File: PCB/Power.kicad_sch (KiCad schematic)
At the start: 19 parts, among them U201 TPS5430DDA, U202 XC6206PxxxMR

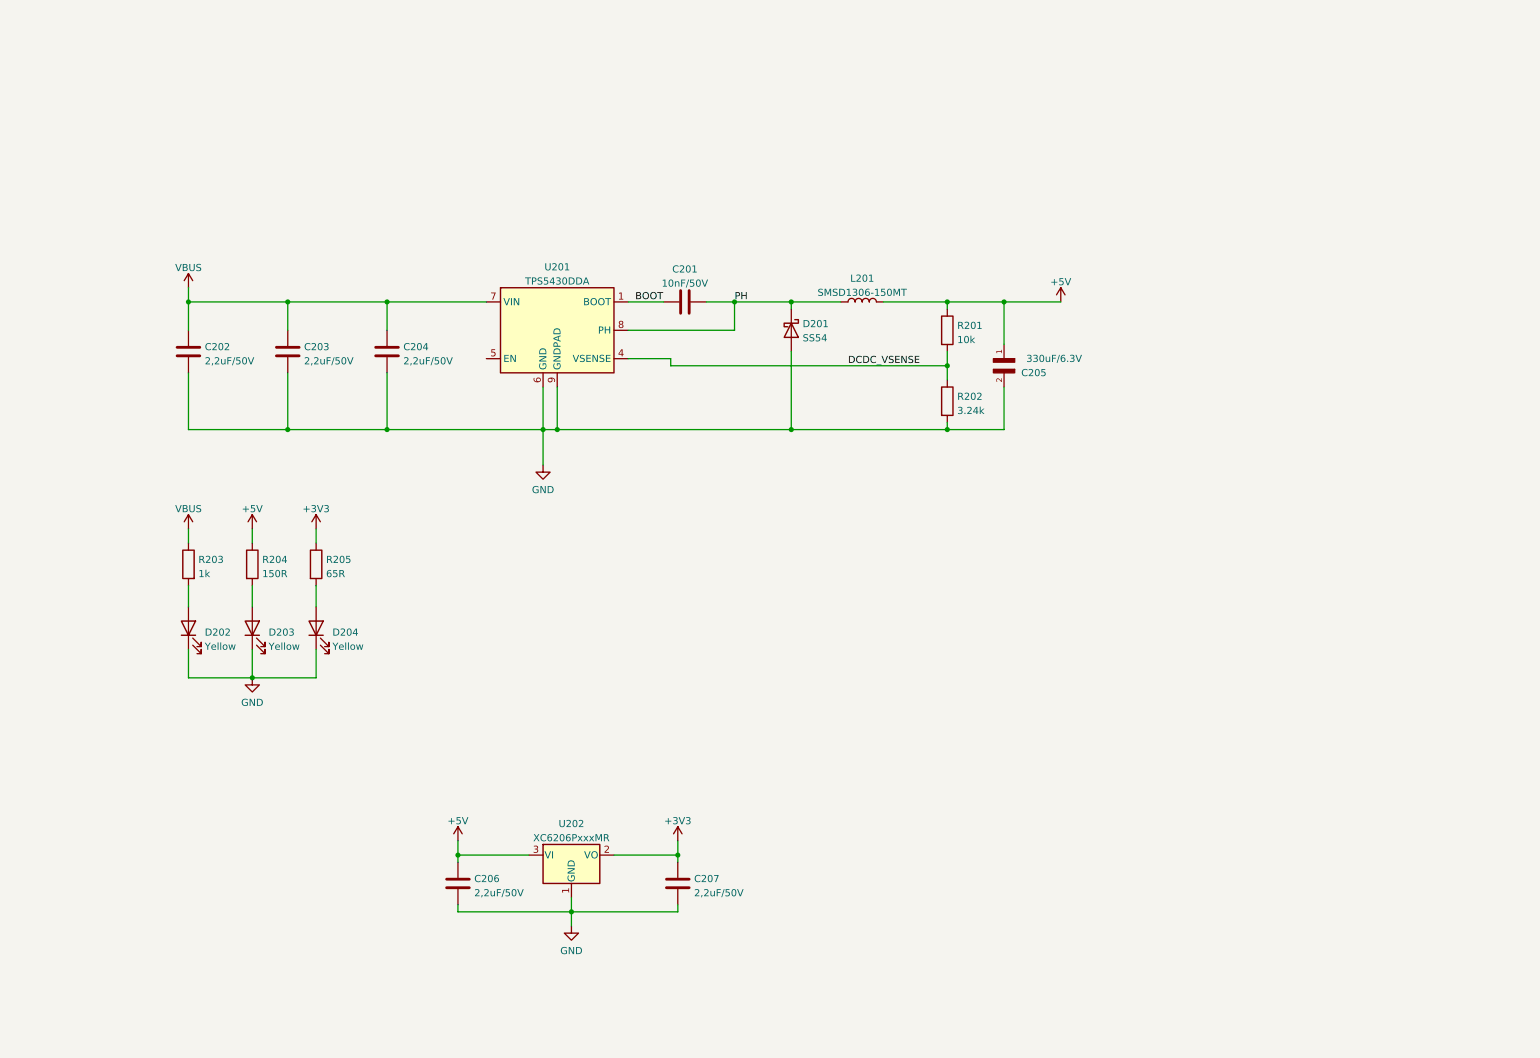
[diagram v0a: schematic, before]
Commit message: Add a new DC/DC solution to the schematic
Components has been added to layout, but not properly done
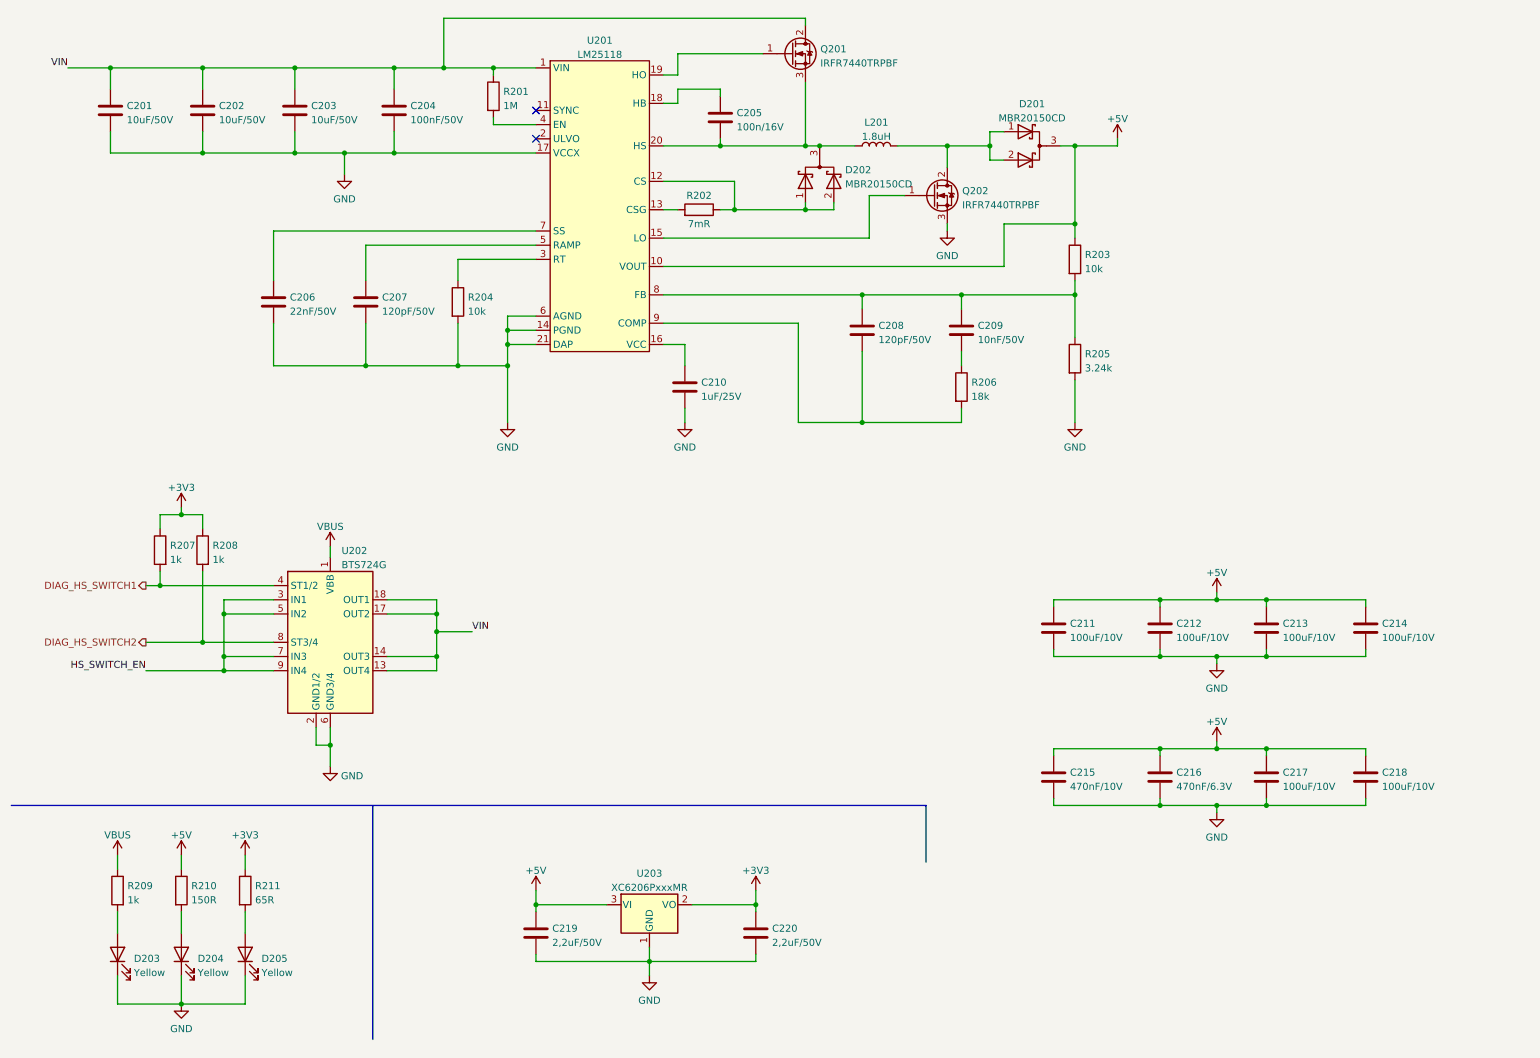
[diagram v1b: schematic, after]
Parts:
- removed C205: 330uF/6.3V, CAPPM7343X310N, symbol Skrooter_symbols:T520D337M006ATE025
- removed D201: SS54, Diode_SMD:D_SMA, symbol Device:D_Schottky
- removed U201: TPS5430DDA, Package_SO:TI_SO-PowerPAD-8_ThermalVias, symbol Regulator_Switching:TPS5430DDA
- added C205: 100n/16V, Capacitor_SMD:C_0402_1005Metric, symbol Device:C
- added C206: 22nF/50V, Capacitor_SMD:C_0402_1005Metric, symbol Device:C
- added C207, C208: 120pF/50V, Capacitor_SMD:C_0402_1005Metric, symbol Device:C
- added C209: 10nF/50V, Capacitor_SMD:C_0402_1005Metric, symbol Device:C
- added C210: 1uF/25V, Capacitor_SMD:C_0402_1005Metric, symbol Device:C
- added C211, C212, C213, C214, C217, C218: 100uF/10V, Capacitor_SMD:C_1206_3216Metric, symbol Device:C
- added C215: 470nF/10V, Capacitor_SMD:C_0402_1005Metric, symbol Device:C
- added C216: 470nF/6.3V, Capacitor_SMD:C_0402_1005Metric, symbol Device:C
- added D201, D202: MBR20150CD, Package_TO_SOT_SMD:TO-252-2, symbol Device:D_Schottky_Dual_CommonCathode_AAK_Parallel
- added Q201, Q202: IRFR7440TRPBF, Package_TO_SOT_SMD:TO-252-2, symbol Device:Q_NMOS_GDS
- added R203, R204: 10k, Resistor_SMD:R_0402_1005Metric, symbol Device:R
- added R205: 3.24k, Resistor_SMD:R_0402_1005Metric, symbol Device:R
- added R206: 18k, Resistor_SMD:R_0402_1005Metric, symbol Device:R
- added R207, R208: 1k, Resistor_SMD:R_0402_1005Metric, symbol Device:R
- added U201: LM25118, Package_SO:HTSSOP-20-1EP_4.4x6.5mm_P0.65mm_EP3.4x6.5mm_Mask2.75x3.43mm_ThermalVias, symbol Skrooter_symbols:LM25118
- added U202: BTS724G, Package_SO:Infineon_PG-DSO-20-32, symbol Power_Management:BTS724G
- C201: value 10nF/50V -> 10uF/50V; footprint Capacitor_SMD:C_0402_1005Metric -> Capacitor_SMD:C_0805_2012Metric; LCSC C15195 -> C440198
- C202, C203: value 2,2uF/50V -> 10uF/50V; LCSC C49217 -> C440198
- C204: value 2,2uF/50V -> 100nF/50V; footprint Capacitor_SMD:C_0805_2012Metric -> Capacitor_SMD:C_0402_1005Metric; LCSC C49217 -> C307331
- D203: renamed from D202; LCSC (none) -> C72038
- D204: renamed from D203; LCSC (none) -> C72038
- D205: renamed from D204; LCSC (none) -> C72038
- L201: value SMSD1306-150MT -> 1.8uH; footprint Inductor_SMD:L_Bourns_SDR1806 -> Inductor_SMD:L_12x12mm_H8mm; LCSC C33624 -> C718301
- R201: value 10k -> 1M; LCSC C25744 -> C26083
- R202: value 3.24k -> 7mR; footprint Resistor_SMD:R_0402_1005Metric -> Resistor_SMD:R_2512_6332Metric; LCSC C25890 -> C728341
- renumbered C206 to C219, C207 to C220, R203 to R209, R204 to R210, R205 to R211, U202 to U203
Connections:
- net +3V3: now also R207.1, R208.1
- net +5V: now also C211.1, C212.1, C213.1, C214.1, C215.1, C216.1, C217.1, C218.1, D201.3 (A), R203.1, U201.10 (VOUT); no longer L201.2, R201.1
- net GND: now also C201.2, C206.2, C207.2, C210.2, C211.2, C212.2, C213.2, C214.2, C215.2, C216.2, C217.2, C218.2, Q202.3 (S), R204.2, R205.2, U201.14 (PGND), U201.17 (VCCX), U201.21 (DAP), U201.6 (AGND), U202.2 (GND1/2), U202.6 (GND3/4); no longer R202.2
- net VBUS: now also U202.1 (VBB), U202.10 (VBB), U202.11 (VBB), U202.12 (VBB), U202.15 (VBB), U202.16 (VBB), U202.19 (VBB), U202.20 (VBB); no longer C202.1, C203.1, C204.1
- net BOOT renamed VIN
- net VIN: now also C202.1, C203.1, C204.1, R201.1, Q201.2 (D), U201.1 (VIN), U202.13 (OUT4), U202.14 (OUT3), U202.17 (OUT2), U202.18 (OUT1)
- net DCDC_VSENSE: no longer names the net of R202.1
- net DCDC_VSENSE: now also D202.1 (K), D202.2 (K), U201.12 (CS); no longer R201.2
- net PH: no longer names the net of L201.1
- net PH: now also C205.2, D202.3 (A), Q201.3 (S), U201.20 (HS); no longer C201.2
- new net: D201.1 (K), D201.2 (K), L201.2, Q202.2 (D)
- new net: C208.1, C209.1, R203.2, R205.1, U201.8 (FB)
- new net: Q202.1 (G), U201.15 (LO)
- new net: C208.2, R206.2, U201.9 (COMP)
- new net: C209.2, R206.1
- new net: C207.1, U201.5 (RAMP)
- new net: R202.2, U201.13 (CSG)
- new net: R204.1, U201.3 (RT)
- new net: C205.1, U201.18 (HB)
- new net: C206.1, U201.7 (SS)
- new net: C210.1, U201.16 (VCC)
- new net: R201.2, U201.4 (EN)
- new net: Q201.1 (G), U201.19 (HO)
- new net DIAG_HS_SWITCH1: R207.2, U202.4 (ST1/2)
- new net DIAG_HS_SWITCH2: R208.2, U202.8 (ST3/4)
- new net HS_SWITCH_EN: U202.3 (IN1), U202.5 (IN2), U202.7 (IN3), U202.9 (IN4)
- no-connect marks 0 -> 2
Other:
- moved on the sheet: C219, C220, D203, D204, D205, R209, R210, R211, U203

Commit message: reroute pretty much everything
Routing is done for new DC/DC!
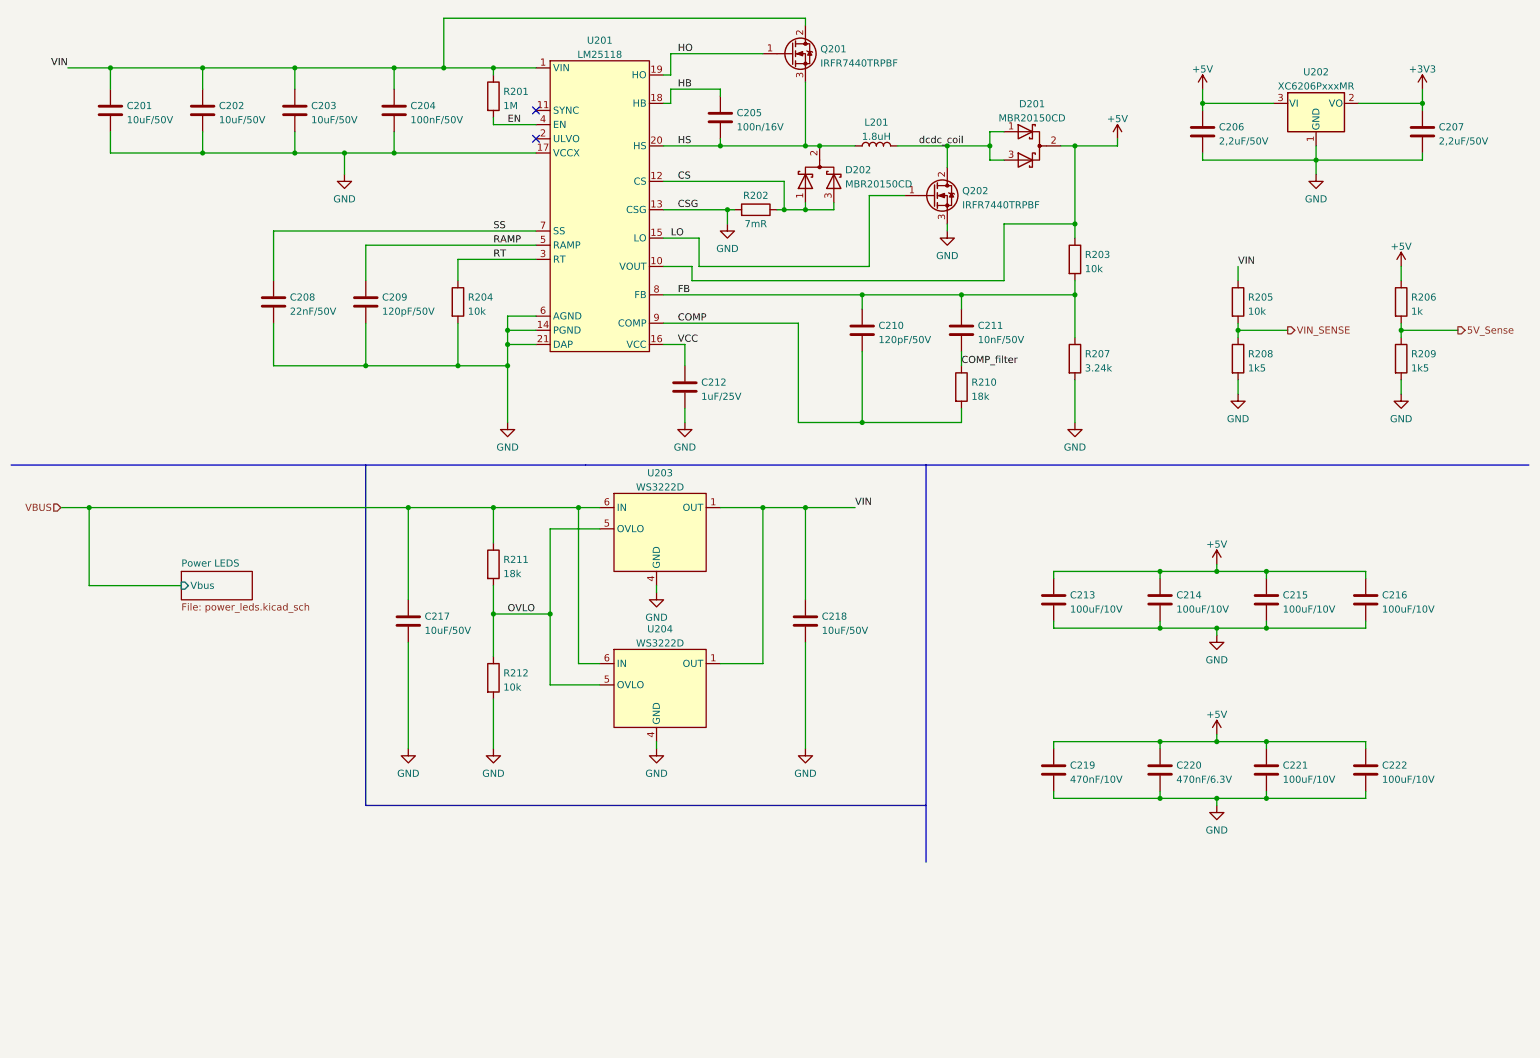
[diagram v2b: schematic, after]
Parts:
- removed D203, D204, D205: Yellow, LED_SMD:LED_0603_1608Metric, symbol Device:LED
- removed R207: 1k, Resistor_SMD:R_0402_1005Metric, symbol Device:R
- removed R210: 150R, Resistor_SMD:R_0402_1005Metric, symbol Device:R
- removed U202: BTS724G, Package_SO:Infineon_PG-DSO-20-32, symbol Power_Management:BTS724G
- added C217, C218: 10uF/50V, Capacitor_SMD:C_0805_2012Metric, symbol Device:C
- added R205, R212: 10k, Resistor_SMD:R_0402_1005Metric, symbol Device:R
- added R206: 1k, Resistor_SMD:R_0402_1005Metric, symbol Device:R
- added U203, U204: WS3222D, Package_DFN_QFN:WDFN-8-1EP_2x2mm_P0.5mm_EP0.8x1.2mm, symbol Skrooter_symbols:WS3222D
- D201, D202: symbol Device:D_Schottky_Dual_CommonCathode_AAK_Parallel -> Device:D_Schottky_Dual_CommonCathode_AKA_Parallel
- R208, R209: value 1k -> 1k5; LCSC C11702 -> C105871
- R211: value 65R -> 18k; footprint Resistor_SMD:R_0603_1608Metric -> Resistor_SMD:R_0402_1005Metric; LCSC C27592 -> C25762
- renumbered C219 to C206, C220 to C207, C206 to C208, C207 to C209, C208 to C210, C209 to C211, C210 to C212, C211 to C213, C212 to C214, C213 to C215, C214 to C216, C215 to C219, C216 to C220, C217 to C221, C218 to C222, R205 to R207, R206 to R210, U203 to U202
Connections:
- net DIAG_HS_SWITCH2 is gone; now on net GND: R208.2
- net +3V3: no longer R208.1, R211.1
- net +5V: now also D201.2 (A), R206.1; no longer D201.3 (A)
- net GND: now also R202.2, R209.2, U201.13 (CSG), C217.2, C218.2, R212.2, U203.4 (GND), U203.9 (GND), U204.4 (GND), U204.9 (GND)
- net VIN: now also C218.1, R205.1, U203.1 (OUT), U203.2 (OUT), U203.3 (OUT), U204.1 (OUT), U204.2 (OUT), U204.3 (OUT)
- net dcdc_coil: now reaches D201.1 (K), L201.2, Q202.2 (D)
- net dcdc_coil: now also D201.3 (K); no longer D201.2 (K)
- net FB: now reaches C210.1, C211.1, R203.2, R207.1, U201.8 (FB)
- net LO: now reaches Q202.1 (G), U201.15 (LO)
- net HS: now reaches C205.2, L201.1, Q201.3 (S), U201.20 (HS)
- net HS: now also D202.2 (A); no longer D202.3 (A)
- net COMP: now reaches C210.2, R210.2, U201.9 (COMP)
- net CS: now reaches D202.1 (K), R202.1, U201.12 (CS)
- net CS: now also D202.3 (K); no longer D202.2 (K)
- net OVLO: now reaches R211.2
- net OVLO: now also R212.1, U203.5 (OVLO), U204.5 (OVLO)
- net COMP_filter: now reaches C211.2, R210.1
- net RAMP: now reaches C209.1, U201.5 (RAMP)
- net RT: now reaches R204.1, U201.3 (RT)
- net HB: now reaches C205.1, U201.18 (HB)
- net SS: now reaches C208.1, U201.7 (SS)
- net VCC: now reaches C212.1, U201.16 (VCC)
- net EN: now reaches R201.2, U201.4 (EN)
- net HO: now reaches Q201.1 (G), U201.19 (HO)
- net VBUS renamed 5V_Sense
- net 5V_Sense: now also R206.2
- new net IN: C217.1, R211.1, U203.6 (IN), U203.7 (IN), U203.8 (IN), U204.6 (IN), U204.7 (IN), U204.8 (IN)
- new net VIN_SENSE: R205.2, R208.1
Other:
- added sheet Power LEDS (power_leds.kicad_sch)
- moved on the sheet: C206, C207, C213, C214, C215, C216, C219, C220, C221, C222, R202, U202

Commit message: Add LEDs for each USBPD level and a microphone
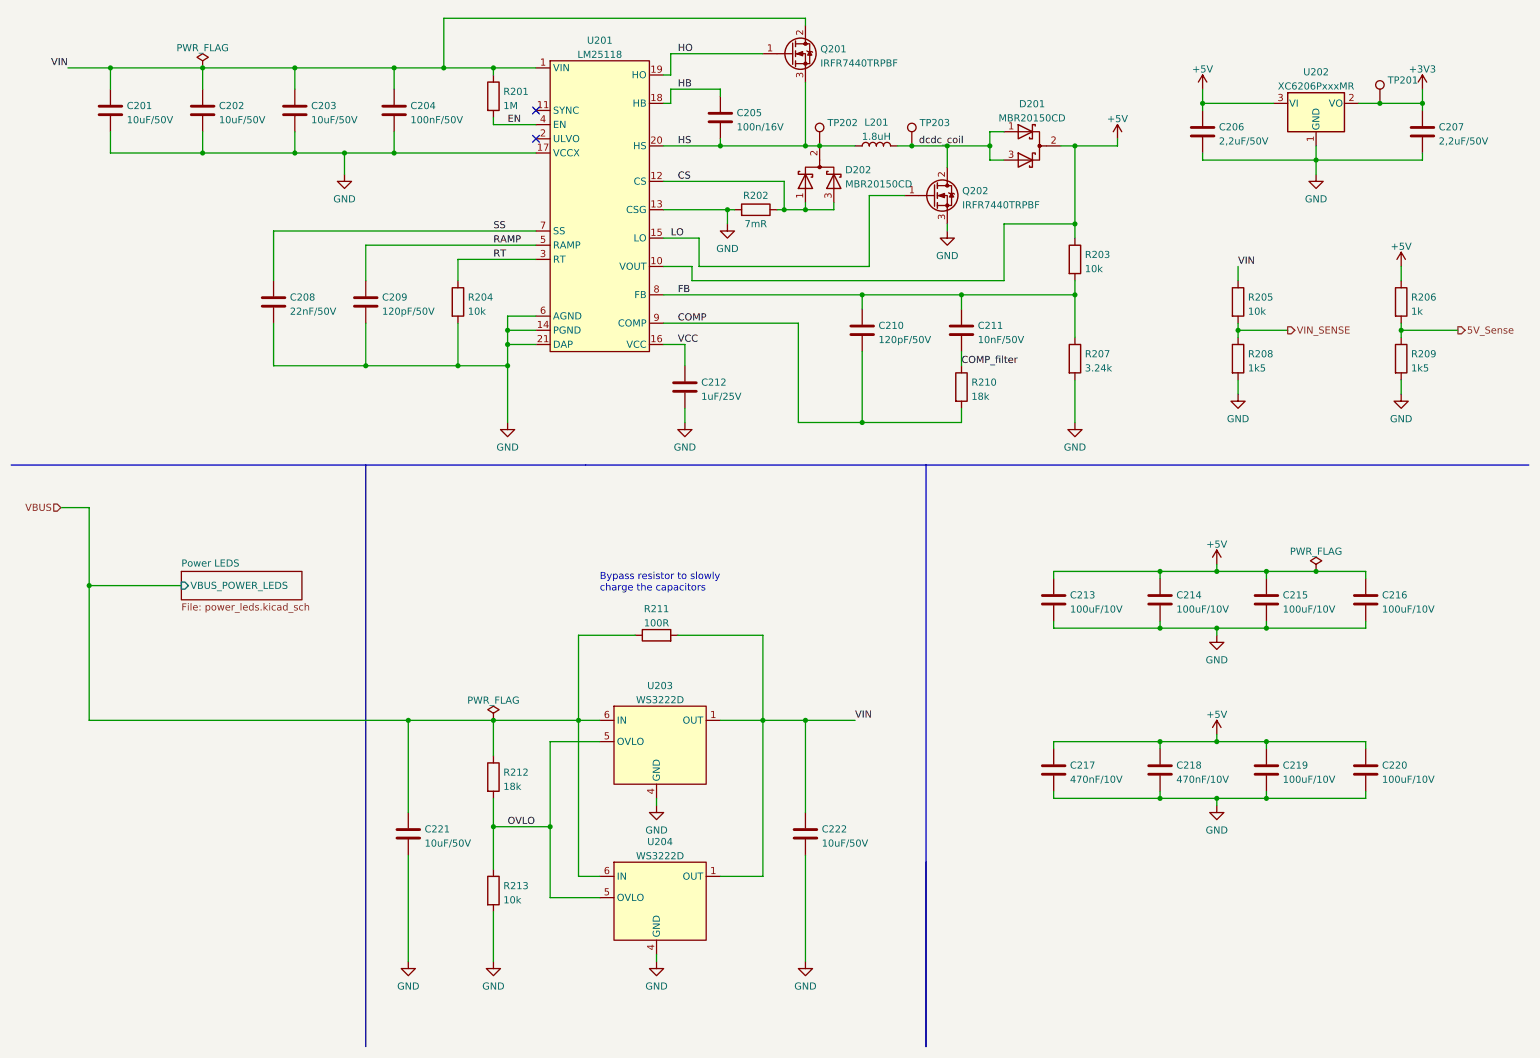
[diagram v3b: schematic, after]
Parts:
- added R211: 100R, Resistor_SMD:R_1206_3216Metric, symbol Device:R
- added TP201, TP202, TP203: TestPoint, TestPoint:TestPoint_Keystone_5000-5004_Miniature, symbol Connector:TestPoint
- C218: renamed from C220; value 470nF/6.3V -> 470nF/10V
- renumbered C219 to C217, C221 to C219, C222 to C220, C217 to C221, C218 to C222, R211 to R212, R212 to R213
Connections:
- net +3V3: now also TP201.1
- net HS: now also TP202.1
- net IN: now also R211.1
- net VIN: now also R211.2
- net dcdc_coil: now also TP203.1
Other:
- sheet Power LEDS ports: added VBUS_POWER_LEDS; removed Vbus
- note added: "Bypass resistor to slowly charge the capacitors"
- moved on the sheet: C221, C222, R212, R213, U203, U204

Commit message: Fix review comments
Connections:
- net GND: no longer R213.2
- new net ~{HSW_EN}: R213.2
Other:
- moved on the sheet: C206, C207, C221, TP201, U202
